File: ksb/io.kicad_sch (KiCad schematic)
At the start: 11 parts, among them U4 X850744-001

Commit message: Internal Connectors
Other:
- moved on the sheet: C362, C363, C364, C365

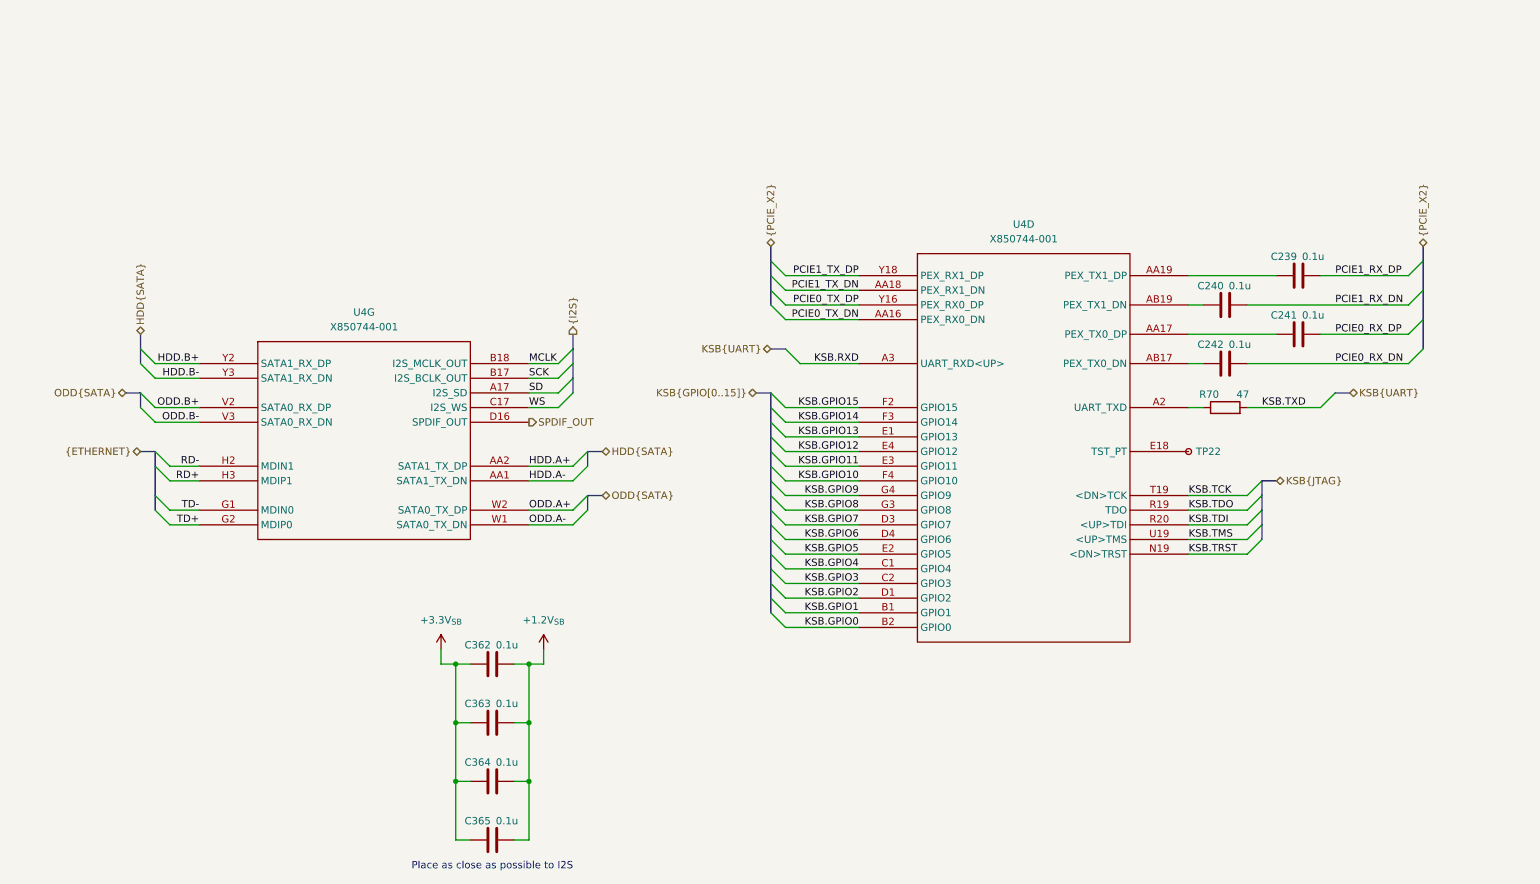
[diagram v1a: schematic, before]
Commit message: Multipurpose and standby power rails, Reannotated schematic
Added V_1P2, V_1P8, V_5P0DUAL, V_EFUSE, V_GPUPCIE, V_3P3STBY and V_1P2STBY
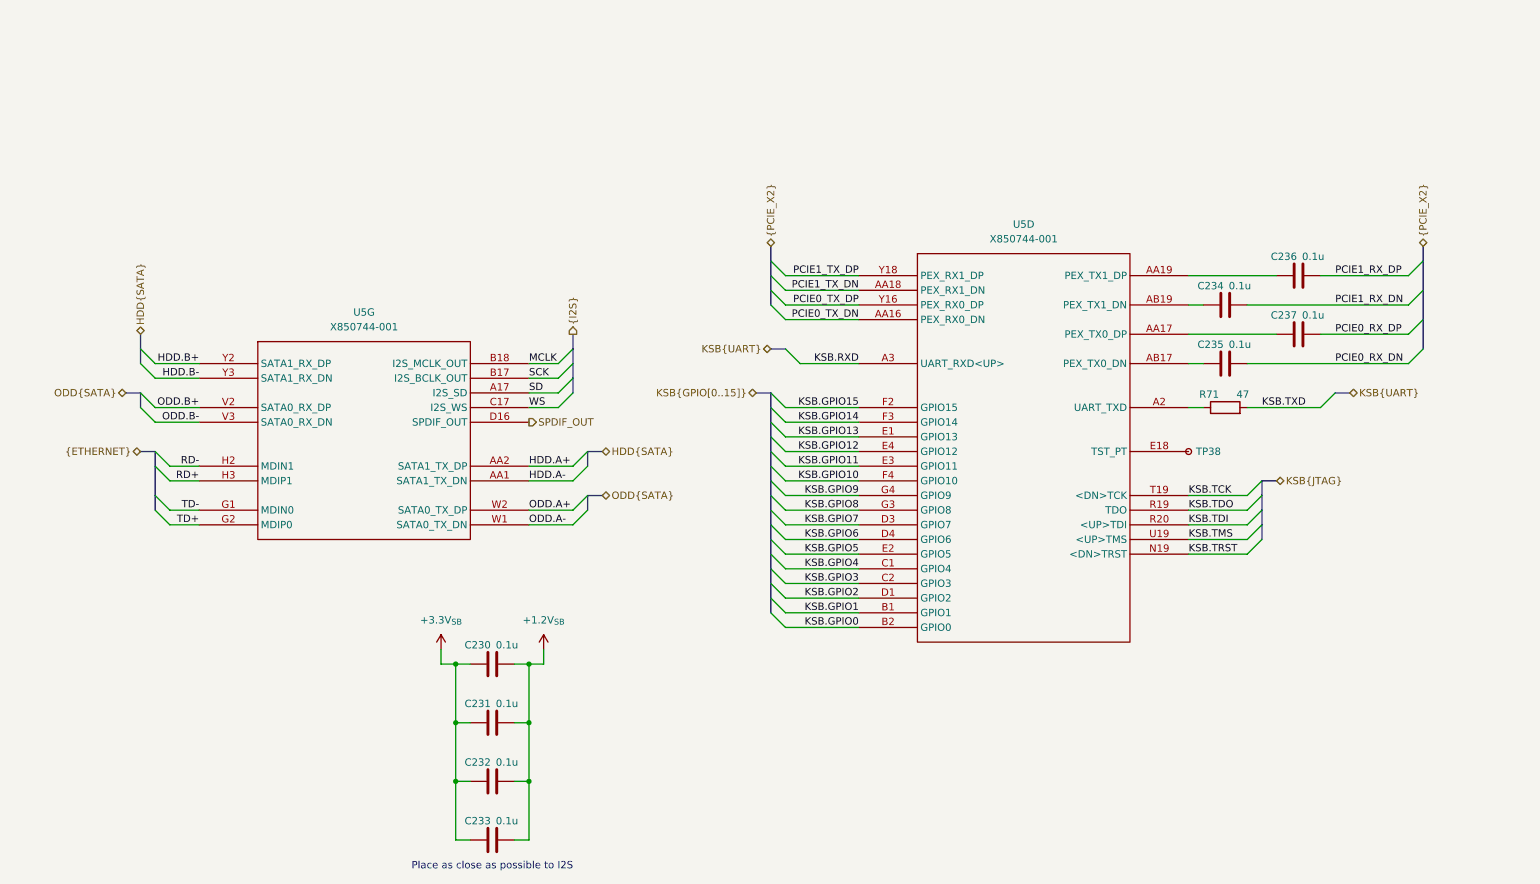
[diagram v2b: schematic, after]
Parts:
- renumbered C362 to C230, C363 to C231, C364 to C232, C365 to C233, C240 to C234, C242 to C235, C239 to C236, C241 to C237, R70 to R71, TP22 to TP38, U4 to U5
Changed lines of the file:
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@@
 		(dnp no)
 		(fields_autoplaced yes)
-		(property "Reference" "U4"
+		(property "Reference" "U5"
 			(at 191.135 55.88 0)
 			(effects
@@
 			(project ""
 				(path "/16640ecb-e4a4-4594-871b-70047bfba6e0/5578fb0d-7a85-48a3-97bd-11e67ac7c8dc/21e99fed-fcc4-453b-9dd2-fd37399cf641"
-					(reference "U4")
+					(reference "U5")
 					(unit 4)
 				)
@@
 		(dnp no)
 		(fields_autoplaced yes)
-		(property "Reference" "#PWR099"
+		(property "Reference" "#PWR0111"
 			(at 90.17 133.35 0)
 			(effects
@@
 			(project "StingBurst"
 				(path "/16640ecb-e4a4-4594-871b-70047bfba6e0/5578fb0d-7a85-48a3-97bd-11e67ac7c8dc/21e99fed-fcc4-453b-9dd2-fd37399cf641"
-					(reference "#PWR099")
+					(reference "#PWR0111")
 					(unit 1)
 				)
@@
 		(on_board yes)
 		(dnp no)
-		(property "Reference" "C242"
+		(property "Reference" "C235"
 			(at 223.52 76.708 90)
 			(effects
@@
 			(project "StingBurst"
 				(path "/16640ecb-e4a4-4594-871b-70047bfba6e0/5578fb0d-7a85-48a3-97bd-11e67ac7c8dc/21e99fed-fcc4-453b-9dd2-fd37399cf641"
-					(reference "C242")
+					(reference "C235")
 					(unit 1)
 				)
@@
 		(on_board yes)
 		(dnp no)
-		(property "Reference" "C363"
+		(property "Reference" "C231"
 			(at 96.52 138.938 90)
 			(effects
@@
 			(project "StingBurst"
 				(path "/16640ecb-e4a4-4594-871b-70047bfba6e0/5578fb0d-7a85-48a3-97bd-11e67ac7c8dc/21e99fed-fcc4-453b-9dd2-fd37399cf641"
-					(reference "C363")
+					(reference "C231")
 					(unit 1)
 				)
@@
 		(dnp no)
 		(fields_autoplaced yes)
-		(property "Reference" "U4"
+		(property "Reference" "U5"
 			(at 76.835 71.12 0)
 			(effects
@@
 			(project ""
 				(path "/16640ecb-e4a4-4594-871b-70047bfba6e0/5578fb0d-7a85-48a3-97bd-11e67ac7c8dc/21e99fed-fcc4-453b-9dd2-fd37399cf641"
-					(reference "U4")
+					(reference "U5")
 					(unit 7)
 				)
@@
 		(on_board yes)
 		(dnp no)
-		(property "Reference" "C362"
+		(property "Reference" "C230"
 			(at 96.52 128.778 90)
 			(effects
@@
 			(project "StingBurst"
 				(path "/16640ecb-e4a4-4594-871b-70047bfba6e0/5578fb0d-7a85-48a3-97bd-11e67ac7c8dc/21e99fed-fcc4-453b-9dd2-fd37399cf641"
-					(reference "C362")
+					(reference "C230")
 					(unit 1)
 				)
@@
 		(on_board yes)
 		(dnp no)
-		(property "Reference" "TP22"
+		(property "Reference" "TP38"
 			(at 220.98 95.25 0)
 			(effects
@@
 			(project "StingBurst"
 				(path "/16640ecb-e4a4-4594-871b-70047bfba6e0/5578fb0d-7a85-48a3-97bd-11e67ac7c8dc/21e99fed-fcc4-453b-9dd2-fd37399cf641"
-					(reference "TP22")
+					(reference "TP38")
 					(unit 1)
 				)
@@
 		(on_board yes)
 		(dnp no)
-		(property "Reference" "C364"
+		(property "Reference" "C232"
 			(at 96.52 149.098 90)
 			(effects
@@
 			(project "StingBurst"
 				(path "/16640ecb-e4a4-4594-871b-70047bfba6e0/5578fb0d-7a85-48a3-97bd-11e67ac7c8dc/21e99fed-fcc4-453b-9dd2-fd37399cf641"
-					(reference "C364")
+					(reference "C232")
 					(unit 1)
 				)
@@
 		(on_board yes)
 		(dnp no)
-		(property "Reference" "C365"
+		(property "Reference" "C233"
 			(at 96.52 159.258 90)
 			(effects
@@
 			(project "StingBurst"
 				(path "/16640ecb-e4a4-4594-871b-70047bfba6e0/5578fb0d-7a85-48a3-97bd-11e67ac7c8dc/21e99fed-fcc4-453b-9dd2-fd37399cf641"
-					(reference "C365")
+					(reference "C233")
 					(unit 1)
 				)
@@
 		(on_board yes)
 		(dnp no)
-		(property "Reference" "C239"
+		(property "Reference" "C236"
 			(at 236.22 61.468 90)
 			(effects
@@
 			(project "StingBurst"
 				(path "/16640ecb-e4a4-4594-871b-70047bfba6e0/5578fb0d-7a85-48a3-97bd-11e67ac7c8dc/21e99fed-fcc4-453b-9dd2-fd37399cf641"
-					(reference "C239")
+					(reference "C236")
 					(unit 1)
 				)
@@
 		(on_board yes)
 		(dnp no)
-		(property "Reference" "C241"
+		(property "Reference" "C237"
 			(at 236.22 71.628 90)
 			(effects
@@
 			(project "StingBurst"
 				(path "/16640ecb-e4a4-4594-871b-70047bfba6e0/5578fb0d-7a85-48a3-97bd-11e67ac7c8dc/21e99fed-fcc4-453b-9dd2-fd37399cf641"
-					(reference "C241")
+					(reference "C237")
 					(unit 1)
 				)
@@
 		(dnp no)
 		(fields_autoplaced yes)
-		(property "Reference" "#PWR0173"
+		(property "Reference" "#PWR0112"
 			(at 107.95 133.35 0)
 			(effects
@@
 			(project ""
 				(path "/16640ecb-e4a4-4594-871b-70047bfba6e0/5578fb0d-7a85-48a3-97bd-11e67ac7c8dc/21e99fed-fcc4-453b-9dd2-fd37399cf641"
-					(reference "#PWR0173")
+					(reference "#PWR0112")
 					(unit 1)
 				)
@@
 		(on_board yes)
 		(dnp no)
-		(property "Reference" "R70"
+		(property "Reference" "R71"
 			(at 223.266 85.344 90)
 			(effects
@@
 			(project "StingBurst"
 				(path "/16640ecb-e4a4-4594-871b-70047bfba6e0/5578fb0d-7a85-48a3-97bd-11e67ac7c8dc/21e99fed-fcc4-453b-9dd2-fd37399cf641"
-					(reference "R70")
+					(reference "R71")
 					(unit 1)
 				)
@@
 		(on_board yes)
 		(dnp no)
-		(property "Reference" "C240"
+		(property "Reference" "C234"
 			(at 223.52 66.548 90)
 			(effects
@@
 			(project "StingBurst"
 				(path "/16640ecb-e4a4-4594-871b-70047bfba6e0/5578fb0d-7a85-48a3-97bd-11e67ac7c8dc/21e99fed-fcc4-453b-9dd2-fd37399cf641"
-					(reference "C240")
+					(reference "C234")
 					(unit 1)
 				)
